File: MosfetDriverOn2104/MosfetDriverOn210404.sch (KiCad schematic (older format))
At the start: 39 parts, among them J1 Screw_Terminal_01x02, Q1 IRF540N, Q2 IRF540N, U1 IR2104

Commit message: schematic file updated
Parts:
- removed C? (x2): C, Capacitor_SMD:C_0805_2012Metric, symbol Device:C
- removed C?: CP, Capacitor_SMD:CP_Elec_6.3x5.7, symbol Device:CP
- removed D4: LED, LED_THT:LED_D4.0mm, symbol Device:LED
- removed R3: R, Resistor_THT:R_Axial_DIN0207_L6.3mm_D2.5mm_P7.62mm_Horizontal, symbol Device:R
- removed U?: ATmega328P-AU, Package_QFP:TQFP-32_7x7mm_P0.8mm, symbol MCU_Microchip_ATmega:ATmega328P-AU
- added C1, C2: C_Small, Capacitor_SMD:C_0805_2012Metric, symbol Device:C_Small
- added C3: CP_Small, Capacitor_SMD:C_0805_2012Metric, symbol Device:CP_Small
- added D10, D11: 5.1V, Diodes_SMD:D_SMA, symbol Device:D_Zener_Small
- added D5, D6, D7, D8: LED, LEDs:LED_0805_HandSoldering, symbol Device:LED
- added D9: POWER_LED, LEDs:LED_0805_HandSoldering, symbol Device:LED
- added J10: CROSS CONN, Pin_Headers:Pin_Header_Straight_2x02_Pitch2.54mm_SMD, symbol Connector_Generic:Conn_02x02_Odd_Even
- added J11: Screw_Terminal_01x03, TerminalBlock:TerminalBlock_Altech_AK300-3_P5.00mm, symbol Connector:Screw_Terminal_01x03
- added J2: AVR-ISP-6, Pin_Headers:Pin_Header_Straight_2x03_Pitch2.54mm_SMD, symbol Connector:AVR-ISP-6
- added J3, J4, J6: I2C HDR, Pin_Headers:Pin_Header_Straight_1x04_Pitch2.54mm_SMD_Pin1Right, symbol Connector:Conn_01x04_Male
- added J5: UART HDR, Pin_Headers:Pin_Header_Straight_1x04_Pitch2.54mm_SMD_Pin1Right, symbol Connector:Conn_01x04_Male
- added J7: 5V HDR, Pin_Headers:Pin_Header_Straight_1x04_Pitch2.54mm_SMD_Pin1Right, symbol Connector:Conn_01x04_Male
- added J8: ENCODER HDR, Pin_Headers:Pin_Header_Straight_1x04_Pitch2.54mm_SMD_Pin1Right, symbol Connector:Conn_01x04_Male
- added J9: GND HDR, Pin_Headers:Pin_Header_Straight_1x04_Pitch2.54mm_SMD_Pin1Right, symbol Connector:Conn_01x04_Male
- added R10, R16: 10K, Resistor_SMD:R_0805_2012Metric, symbol Device:R_Small
- added R11, R12, R14, R15, R9: 540, Resistor_SMD:R_0805_2012Metric, symbol Device:R_Small
- added R13, R6: 1K, Resistor_SMD:R_0805_2012Metric, symbol Device:R_Small
- added R5: 10K, Resistor_SMD:R_0805_2012Metric, symbol Device:R
- added R7: 4K7, Resistor_SMD:R_0805_2012Metric, symbol Device:R_Small
- added R8: 4K7, Resistors_SMD:R_0805, symbol Device:R_Small
- added SW1: SW_Push_Dual, Buttons_Switches_SMD:SW_SPST_PTS810, symbol Switch:SW_Push_Dual
- added SW2: SW1, Buttons_Switches_SMD:SW_SPST_PTS810, symbol Switch:SW_Push_Dual
- added SW3: SW2, Buttons_Switches_SMD:SW_SPST_PTS810, symbol Switch:SW_Push_Dual
- added U3: ATmega328P-AU-MCU_Microchip_ATmega, Package_QFP:TQFP-32_7x7mm_P0.8mm, symbol MosfetDriverOn210404-rescue:ATmega328P-AU-MCU_Microchip_ATmega
- added Y1: 16M, symbol Device:Crystal
- gave numbers to parts that had none: 23
- renumbered CB to CB1
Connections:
- net labels added: A, B, M1, M2, MISO, MOSI, RST, RX, SCK, SCL, SDA, SGN1, SGN2, TX
- wire segments 115 -> 230
- no-connect marks 0 -> 8
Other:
- note added: "5V SUPPLY"
- note added: "HALL SENSOR\n"
- note added: "HEADERS"
- note added: "I2C\n"
- note added: "IR2104 AND H BRIDGE"
- note added: "IR2104 SUPPLY"
- note added: "ISP"
- note added: "NEW_Mosfet_Driver"
- note added: "RST CIRC"
- note added: "SWITCHES FOR TESTING\n"
- note added: "TO_CROSS_CONNECTOR"
- note added: "UART\n"
- note added: "USER LED'S\n"
- note added: "uC"
- moved on the sheet: J1

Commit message: #5 fixed, and many other changes.
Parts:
- removed D7, D8: LED, LEDs:LED_0805_HandSoldering, symbol Device:LED
- removed J11: Screw_Terminal_01x03, TerminalBlock:TerminalBlock_Altech_AK300-3_P5.00mm, symbol Connector:Screw_Terminal_01x03
- removed R12, R14, R15: 540, Resistor_SMD:R_0805_2012Metric, symbol Device:R_Small
- removed Y1: 16M, symbol Device:Crystal
- added C10, C9: 22u, Capacitor_SMD:C_0805_2012Metric, symbol Device:CP_Small
- added C8: C_Small, Capacitor_SMD:C_0805_2012Metric, symbol Device:C_Small
- added CB3, CB5: 1uF, symbol Device:C_Small
- added CB4, CB6: .1uF, symbol Device:C_Small
- added D7: 5.1V, Diodes_SMD:D_SMA, symbol Device:D_Zener_Small
- added J11: servo hdr, symbol Connector:Conn_01x03_Male
- added J12: motor, symbol Connector:Screw_Terminal_01x02
- added SW4: SW_DIP_x04, symbol Switch:SW_DIP_x04
- CB1: value 22u -> .1
- CB2: value 22u -> .1u
- R10: value 10K -> 540
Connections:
- net +15V: now also CB3.1, CB4.1, CB5.1, CB6.1
- net +5V: now also SW2.1, SW2.3, U3.2 ([4]PD4), J11.3 (Pin_3), SW4.5, SW4.6, SW4.7, SW4.8; no longer R10.2
- net GND: now also R10.2, C8.2, CB3.2, CB4.2, CB5.2, CB6.2, D7.2 (A), J11.1 (Pin_1)
- net M1: now also J12.2 (Pin_2)
- net M2: now also J12.1 (Pin_1)
- net RST: now also C8.1
- net ~SD: now also U3.11 ([7](AIN1)PD7), D7.1 (K)
- net at CB1.2, U1.6 (VS): now also C9.2
- net at CB1.1, D1.1 (K), U1.8 (VB): now also C9.1
- net at U3.10 ([6](OC0A/AIN0)PD6): no longer D5.2 (A)
- net at D6.2 (A): now also U3.8 (XTAL2/PB7); no longer U3.11 ([7](AIN1)PD7)
- net svo: now reaches U3.12 ([8]PB0)
- net svo: now also J11.2 (Pin_2)
- net at U3.23 ([14](A0)PC0): now also SW4.1
- net at U3.24 ([15](A1)PC1): now also SW4.2
- net at U3.25 ([16](A2)PC2): now also SW4.3
- net at U3.26 ([17](A3)PC3): now also SW4.4
- net at U3.7 (XTAL1/PB6): now also D5.2 (A)
- net at CB2.2, U5.6 (VS): now also C10.2
- net at CB2.1, D14.1 (K), U5.8 (VB): now also C10.1
- net at D6.1 (K): now also R11.1
- net at D5.1 (K): now also R10.1; no longer R11.1
- no-connect marks 8 -> 4
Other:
- note added: "add 5 res's"

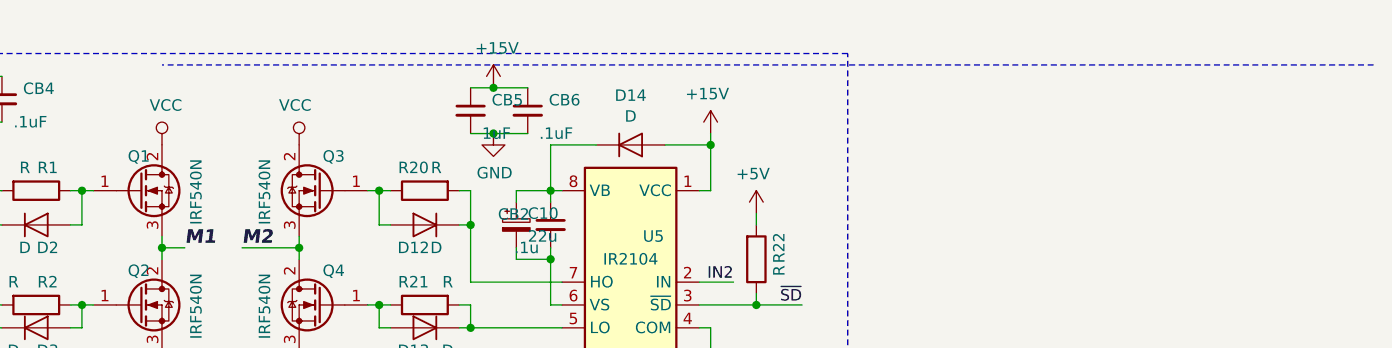
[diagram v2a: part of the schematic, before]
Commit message: #4 fixed
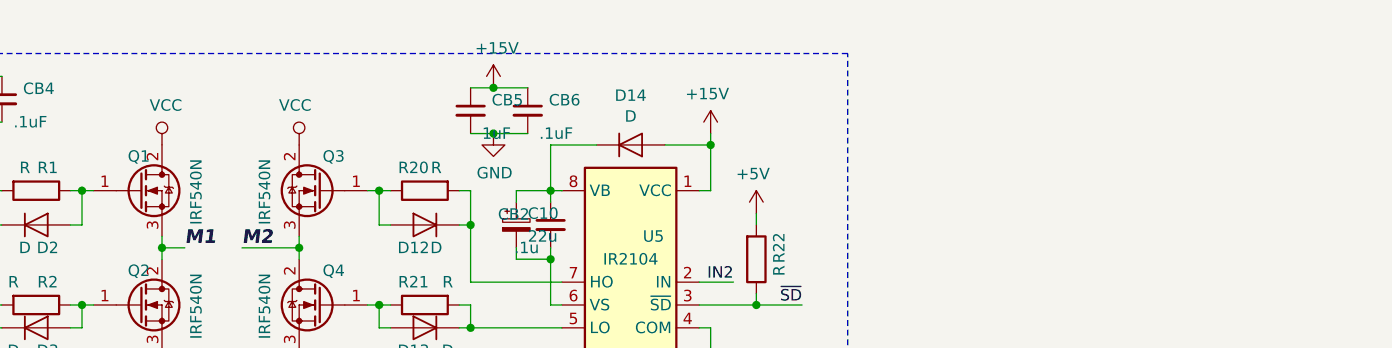
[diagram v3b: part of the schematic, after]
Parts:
- C3: footprint Capacitor_SMD:C_0805_2012Metric -> Capacitor_SMD:CP_Elec_5x4.4
- CB1, CB2, CB3, CB4, CB5, CB6: footprint (none) -> Capacitor_SMD:C_0805_2012Metric
- D5, D6, D9: footprint LEDs:LED_0805_HandSoldering -> LED_SMD:LED_0805_2012Metric
- D7: footprint Diodes_SMD:D_SMA -> LED_SMD:LED_0805_2012Metric
- J10: footprint Pin_Headers:Pin_Header_Straight_2x02_Pitch2.54mm_SMD -> Connector_PinHeader_2.54mm:PinHeader_1x04_P2.54mm_Vertical
- J11: footprint (none) -> TerminalBlock:TerminalBlock_Altech_AK300-3_P5.00mm
- J12: footprint (none) -> TerminalBlock:TerminalBlock_Altech_AK300-2_P5.00mm
- J2: footprint Pin_Headers:Pin_Header_Straight_2x03_Pitch2.54mm_SMD -> Connector_PinHeader_2.54mm:PinHeader_1x04_P2.54mm_Vertical
- J3, J4, J5, J6, J7, J8, J9: footprint Pin_Headers:Pin_Header_Straight_1x04_Pitch2.54mm_SMD_Pin1Right -> Connector_PinHeader_2.54mm:PinHeader_1x04_P2.54mm_Vertical
- SW4: footprint (none) -> Button_Switch_THT:SW_DIP_SPSTx04_Slide_9.78x12.34mm_W7.62mm_P2.54mm
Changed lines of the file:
@@
 F 0 "CB1" H 7042 1496 50  0000 L CNN
 F 1 ".1" H 7000 1350 50  0000 L CNN
-F 2 "" H 6950 1450 50  0001 C CNN
+F 2 "Capacitor_SMD:C_0805_2012Metric" H 6950 1450 50  0001 C CNN
 F 3 "~" H 6950 1450 50  0001 C CNN
 	1    6950 1450
@@
 F 0 "CB2" H 9842 1496 50  0000 L CNN
 F 1 ".1u" H 9800 1350 50  0000 L CNN
-F 2 "" H 9750 1450 50  0001 C CNN
+F 2 "Capacitor_SMD:C_0805_2012Metric" H 9750 1450 50  0001 C CNN
 F 3 "~" H 9750 1450 50  0001 C CNN
 	1    9750 1450
@@
 F 0 "C3" H 1900 1600 50  0000 L CNN
 F 1 "CP_Small" H 1900 1500 50  0000 L CNN
-F 2 "Capacitor_SMD:C_0805_2012Metric" H 1850 1550 50  0001 C CNN
+F 2 "Capacitor_SMD:CP_Elec_5x4.4" H 1850 1550 50  0001 C CNN
 F 3 "~" H 1850 1550 50  0001 C CNN
 	1    1850 1550
@@
 F 0 "J2" H 1650 5550 50  0000 R CNN
 F 1 "AVR-ISP-6" H 2000 5450 50  0000 R CNN
-F 2 "Pin_Headers:Pin_Header_Straight_2x03_Pitch2.54mm_SMD" V 1300 5050 50  0001 C CNN
+F 2 "Connector_PinHeader_2.54mm:PinHeader_1x04_P2.54mm_Vertical" V 1300 5050 50  0001 C CNN
 F 3 " ~" H 275 4450 50  0001 C CNN
 	1    1550 5000
@@
 F 0 "J5" H 3150 4450 50  0000 R CNN
 F 1 "UART HDR" H 3150 4500 50  0000 R CNN
-F 2 "Pin_Headers:Pin_Header_Straight_1x04_Pitch2.54mm_SMD_Pin1Right" H 2800 4950 50  0001 C CNN
+F 2 "Connector_PinHeader_2.54mm:PinHeader_1x04_P2.54mm_Vertical" H 2800 4950 50  0001 C CNN
 F 3 "~" H 2800 4950 50  0001 C CNN
 	1    2800 4950
@@
 F 0 "J3" H 1922 5580 50  0000 R CNN
 F 1 "I2C HDR" H 2100 5400 50  0000 R CNN
-F 2 "Pin_Headers:Pin_Header_Straight_1x04_Pitch2.54mm_SMD_Pin1Right" H 1950 5700 50  0001 C CNN
+F 2 "Connector_PinHeader_2.54mm:PinHeader_1x04_P2.54mm_Vertical" H 1950 5700 50  0001 C CNN
 F 3 "~" H 1950 5700 50  0001 C CNN
 	1    1950 5700
@@
 F 0 "J9" H 4150 4450 50  0000 R CNN
 F 1 "GND HDR" H 4150 4550 50  0000 R CNN
-F 2 "Pin_Headers:Pin_Header_Straight_1x04_Pitch2.54mm_SMD_Pin1Right" H 3800 4950 50  0001 C CNN
+F 2 "Connector_PinHeader_2.54mm:PinHeader_1x04_P2.54mm_Vertical" H 3800 4950 50  0001 C CNN
 F 3 "~" H 3800 4950 50  0001 C CNN
 	1    3800 4950
@@
 F 0 "J7" H 3600 4450 50  0000 R CNN
 F 1 "5V HDR" H 3600 4550 50  0000 R CNN
-F 2 "Pin_Headers:Pin_Header_Straight_1x04_Pitch2.54mm_SMD_Pin1Right" H 3300 5000 50  0001 C CNN
+F 2 "Connector_PinHeader_2.54mm:PinHeader_1x04_P2.54mm_Vertical" H 3300 5000 50  0001 C CNN
 F 3 "~" H 3300 5000 50  0001 C CNN
 	1    3300 5000
@@
 F 0 "D9" V 4388 6832 50  0000 R CNN
 F 1 "POWER_LED" V 4297 6832 50  0000 R CNN
-F 2 "LEDs:LED_0805_HandSoldering" H 4350 6950 50  0001 C CNN
+F 2 "LED_SMD:LED_0805_2012Metric" H 4350 6950 50  0001 C CNN
 F 3 "~" H 4350 6950 50  0001 C CNN
 	1    4350 6950
@@
 F 0 "J4" H 2472 5580 50  0000 R CNN
 F 1 "I2C HDR" H 2650 5400 50  0000 R CNN
-F 2 "Pin_Headers:Pin_Header_Straight_1x04_Pitch2.54mm_SMD_Pin1Right" H 2500 5700 50  0001 C CNN
+F 2 "Connector_PinHeader_2.54mm:PinHeader_1x04_P2.54mm_Vertical" H 2500 5700 50  0001 C CNN
 F 3 "~" H 2500 5700 50  0001 C CNN
 	1    2500 5700
@@
 F 0 "J6" H 3022 5580 50  0000 R CNN
 F 1 "I2C HDR" H 3200 5400 50  0000 R CNN
-F 2 "Pin_Headers:Pin_Header_Straight_1x04_Pitch2.54mm_SMD_Pin1Right" H 3050 5700 50  0001 C CNN
+F 2 "Connector_PinHeader_2.54mm:PinHeader_1x04_P2.54mm_Vertical" H 3050 5700 50  0001 C CNN
 F 3 "~" H 3050 5700 50  0001 C CNN
 	1    3050 5700
@@
 F 0 "J10" H 6350 2717 50  0000 C CNN
 F 1 "CROSS CONN" H 6350 2626 50  0000 C CNN
-F 2 "Pin_Headers:Pin_Header_Straight_2x02_Pitch2.54mm_SMD" H 6300 2500 50  0001 C CNN
+F 2 "Connector_PinHeader_2.54mm:PinHeader_1x04_P2.54mm_Vertical" H 6300 2500 50  0001 C CNN
 F 3 "~" H 6300 2500 50  0001 C CNN
 	1    6300 2500
@@
 F 0 "J8" H 3722 5630 50  0000 R CNN
 F 1 "ENCODER HDR" H 3900 5450 50  0000 R CNN
-F 2 "Pin_Headers:Pin_Header_Straight_1x04_Pitch2.54mm_SMD_Pin1Right" H 3750 5750 50  0001 C CNN
+F 2 "Connector_PinHeader_2.54mm:PinHeader_1x04_P2.54mm_Vertical" H 3750 5750 50  0001 C CNN
 F 3 "~" H 3750 5750 50  0001 C CNN
 	1    3750 5750
@@
 F 0 "J11" H 2650 4300 50  0000 R CNN
 F 1 "servo hdr" H 2550 4300 50  0000 R CNN
-F 2 "" H 2300 4450 50  0001 C CNN
+F 2 "TerminalBlock:TerminalBlock_Altech_AK300-3_P5.00mm" H 2300 4450 50  0001 C CNN
 F 3 "~" H 2300 4450 50  0001 C CNN
 	1    2300 4450
@@
 F 0 "SW4" H 5150 3017 50  0000 C CNN
 F 1 "SW_DIP_x04" H 5150 2926 50  0000 C CNN
-F 2 "" H 5150 2550 50  0001 C CNN
+F 2 "Button_Switch_THT:SW_DIP_SPSTx04_Slide_9.78x12.34mm_W7.62mm_P2.54mm" H 5150 2550 50  0001 C CNN
 F 3 "" H 5150 2550 50  0001 C CNN
 	1    5150 2550
@@
 F 0 "CB3" H 7192 946 50  0000 L CNN
 F 1 "1uF" H 7150 800 50  0000 L CNN
-F 2 "" H 7100 900 50  0001 C CNN
+F 2 "Capacitor_SMD:C_0805_2012Metric" H 7100 900 50  0001 C CNN
 F 3 "~" H 7100 900 50  0001 C CNN
 	1    7100 900
@@
 F 0 "CB4" H 7442 946 50  0000 L CNN
 F 1 ".1uF" H 7400 800 50  0000 L CNN
-F 2 "" H 7350 900 50  0001 C CNN
+F 2 "Capacitor_SMD:C_0805_2012Metric" H 7350 900 50  0001 C CNN
 F 3 "~" H 7350 900 50  0001 C CNN
 	1    7350 900
@@
 Wire Wire Line
 	7200 1000 7350 1000
-Wire Notes Line
-	13350 750  8050 750
 $Comp
 L Device:C_Small CB5
@@
 F 0 "CB5" H 9492 996 50  0000 L CNN
 F 1 "1uF" H 9450 850 50  0000 L CNN
-F 2 "" H 9400 950 50  0001 C CNN
+F 2 "Capacitor_SMD:C_0805_2012Metric" H 9400 950 50  0001 C CNN
 F 3 "~" H 9400 950 50  0001 C CNN
 	1    9400 950
@@
 F 0 "CB6" H 9742 996 50  0000 L CNN
 F 1 ".1uF" H 9700 850 50  0000 L CNN
-F 2 "" H 9650 950 50  0001 C CNN
+F 2 "Capacitor_SMD:C_0805_2012Metric" H 9650 950 50  0001 C CNN
 F 3 "~" H 9650 950 50  0001 C CNN
 	1    9650 950
@@
 F 0 "D5" H 2192 2945 50  0000 C CNN
 F 1 "LED" H 2192 3036 50  0000 C CNN
-F 2 "LEDs:LED_0805_HandSoldering" H 2200 3200 50  0001 C CNN
+F 2 "LED_SMD:LED_0805_2012Metric" H 2200 3200 50  0001 C CNN
 F 3 "~" H 2200 3200 50  0001 C CNN
 	1    2200 3200
@@
 F 0 "D6" H 2192 3045 50  0000 C CNN
 F 1 "LED" H 2192 3136 50  0000 C CNN
-F 2 "LEDs:LED_0805_HandSoldering" H 2200 3300 50  0001 C CNN
+F 2 "LED_SMD:LED_0805_2012Metric" H 2200 3300 50  0001 C CNN
 F 3 "~" H 2200 3300 50  0001 C CNN
 	1    2200 3300
@@
 F 0 "J12" H 9470 2275 50  0000 C CNN
 F 1 "motor" H 9470 2366 50  0000 C CNN
-F 2 "" H 9550 2600 50  0001 C CNN
+F 2 "TerminalBlock:TerminalBlock_Altech_AK300-2_P5.00mm" H 9550 2600 50  0001 C CNN
 F 3 "~" H 9550 2600 50  0001 C CNN
 	1    9550 2600
@@
 F 0 "D7" V 4204 3968 50  0000 L CNN
 F 1 "5.1V" V 4295 3968 50  0000 L CNN
-F 2 "Diodes_SMD:D_SMA" V 4250 3900 50  0001 C CNN
+F 2 "LED_SMD:LED_0805_2012Metric" V 4250 3900 50  0001 C CNN
 F 3 "~" V 4250 3900 50  0001 C CNN
 	1    4250 3900

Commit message: #4 ,switches footprints also changed to THT
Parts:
- SW1, SW2, SW3: footprint Buttons_Switches_SMD:SW_SPST_PTS810 -> Button_Switch_THT:SW_PUSH_6mm
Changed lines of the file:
@@
 F 0 "SW1" H 2650 1335 50  0000 C CNN
 F 1 "SW_Push_Dual" H 2650 1244 50  0000 C CNN
-F 2 "Buttons_Switches_SMD:SW_SPST_PTS810" H 2650 1250 50  0001 C CNN
+F 2 "Button_Switch_THT:SW_PUSH_6mm" H 2650 1250 50  0001 C CNN
 F 3 "" H 2650 1250 50  0001 C CNN
 	1    2650 1050
@@
 F 0 "SW2" H 4750 3685 50  0000 C CNN
 F 1 "SW1" H 4750 3594 50  0000 C CNN
-F 2 "Buttons_Switches_SMD:SW_SPST_PTS810" H 4750 3600 50  0001 C CNN
+F 2 "Button_Switch_THT:SW_PUSH_6mm" H 4750 3600 50  0001 C CNN
 F 3 "" H 4750 3600 50  0001 C CNN
 	1    4750 3400
@@
 F 0 "SW3" H 5300 3985 50  0000 C CNN
 F 1 "SW2" H 5300 3894 50  0000 C CNN
-F 2 "Buttons_Switches_SMD:SW_SPST_PTS810" H 5300 3900 50  0001 C CNN
+F 2 "Button_Switch_THT:SW_PUSH_6mm" H 5300 3900 50  0001 C CNN
 F 3 "" H 5300 3900 50  0001 C CNN
 	1    5300 3700

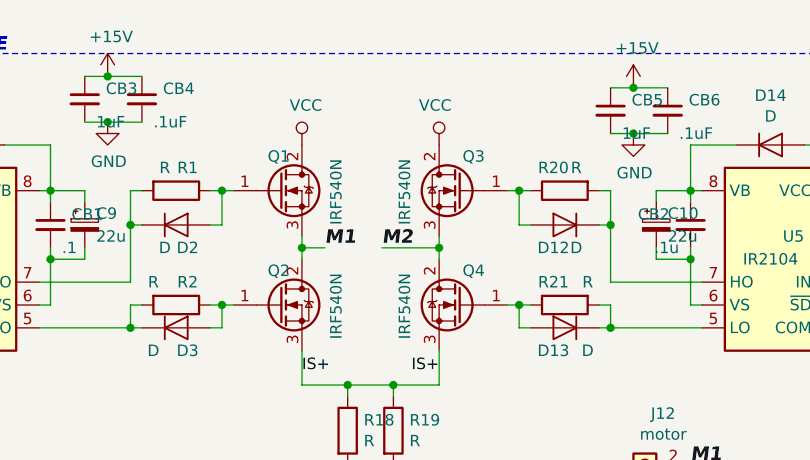
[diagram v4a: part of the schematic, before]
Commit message: Schematcs updated with mosfet footprints
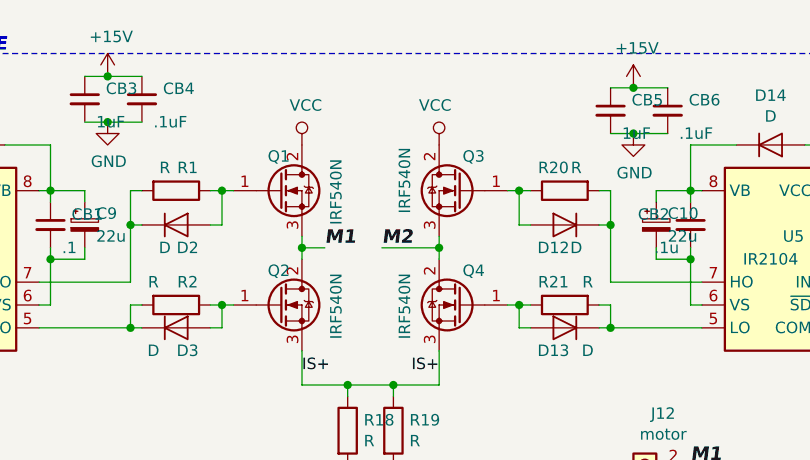
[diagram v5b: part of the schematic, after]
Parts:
- Q1, Q2, Q3, Q4: footprint Package_TO_SOT_THT:TO-220-3_Vertical -> Footprints:TO220_HS_SCREW
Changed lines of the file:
@@
 F 0 "Q1" H 7900 1450 50  0000 L CNN
 F 1 "IRF540N" V 8200 1150 50  0000 L CNN
-F 2 "Package_TO_SOT_THT:TO-220-3_Vertical" H 8200 1225 50  0001 L CIN
+F 2 "Footprints:TO220_HS_SCREW" H 8200 1225 50  0001 L CIN
 F 3 "http://www.irf.com/product-info/datasheets/data/irf540n.pdf" H 7950 1300 50  0001 L CNN
 	1    7950 1300
@@
 F 0 "Q2" H 7900 1950 50  0000 L CNN
 F 1 "IRF540N" V 8200 1650 50  0000 L CNN
-F 2 "Package_TO_SOT_THT:TO-220-3_Vertical" H 8200 1725 50  0001 L CIN
+F 2 "Footprints:TO220_HS_SCREW" H 8200 1725 50  0001 L CIN
 F 3 "http://www.irf.com/product-info/datasheets/data/irf540n.pdf" H 7950 1800 50  0001 L CNN
 	1    7950 1800
@@
 P 8750 1300
 F 0 "Q3" H 8650 1450 50  0000 L CNN
-F 1 "IRF540N" V 9000 1150 50  0000 L CNN
-F 2 "Package_TO_SOT_THT:TO-220-3_Vertical" H 9000 1225 50  0001 L CIN
+F 1 "IRF540N" V 9000 1200 50  0000 L CNN
+F 2 "Footprints:TO220_HS_SCREW" H 9000 1225 50  0001 L CIN
 F 3 "http://www.irf.com/product-info/datasheets/data/irf540n.pdf" H 8750 1300 50  0001 L CNN
 	1    8750 1300
@@
 F 0 "Q4" H 8650 1950 50  0000 L CNN
 F 1 "IRF540N" V 9000 1650 50  0000 L CNN
-F 2 "Package_TO_SOT_THT:TO-220-3_Vertical" H 9000 1725 50  0001 L CIN
+F 2 "Footprints:TO220_HS_SCREW" H 9000 1725 50  0001 L CIN
 F 3 "http://www.irf.com/product-info/datasheets/data/irf540n.pdf" H 8750 1800 50  0001 L CNN
 	1    8750 1800
